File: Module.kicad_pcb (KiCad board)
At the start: 6 copper layers, 30 x 41.8 mm, 128 parts

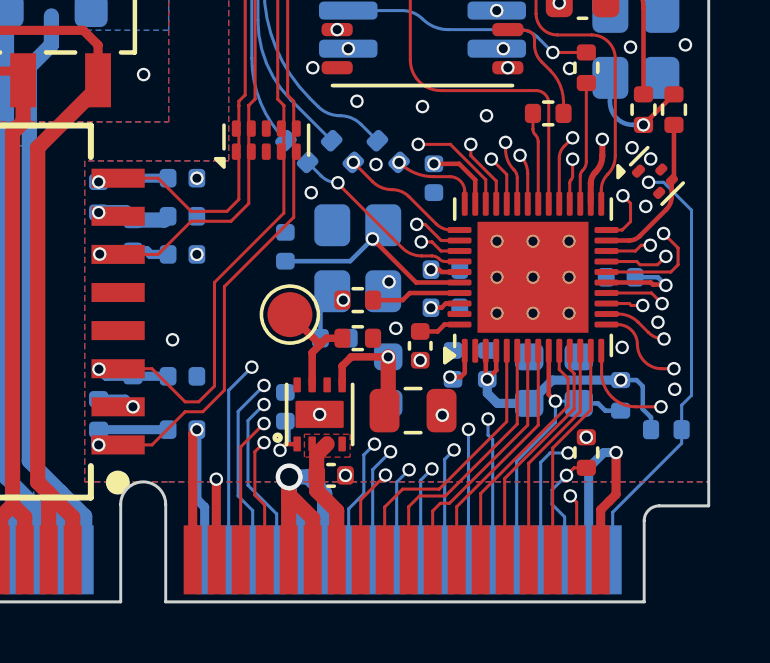
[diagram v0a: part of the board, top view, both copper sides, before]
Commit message: increased trace width from all goldfinger connector traces to 6mil reduced mask and paste reduction of 1U3 to 1mil
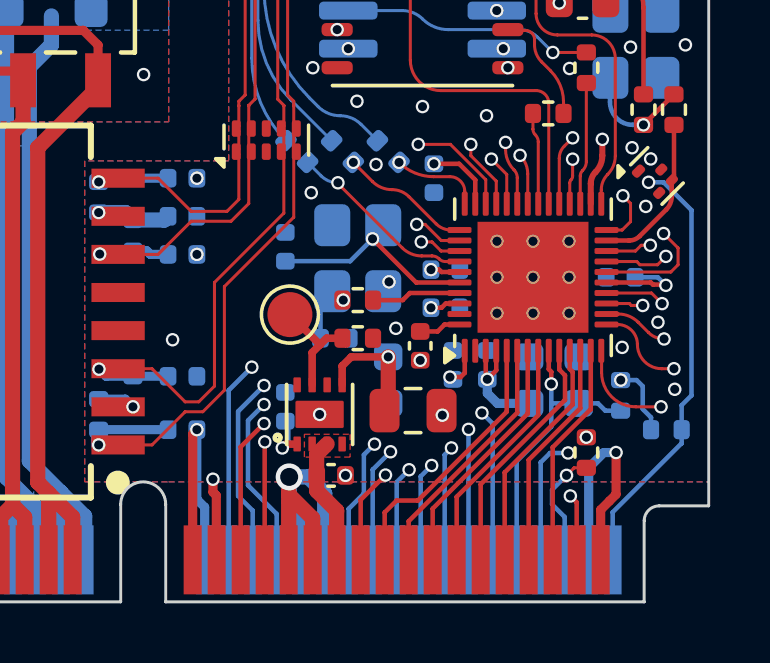
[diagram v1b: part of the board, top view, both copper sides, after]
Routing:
- net +3.3V: track 30.6 -> 27.2 mm
- net /GPIO37: track 8.98 -> 8.47 mm

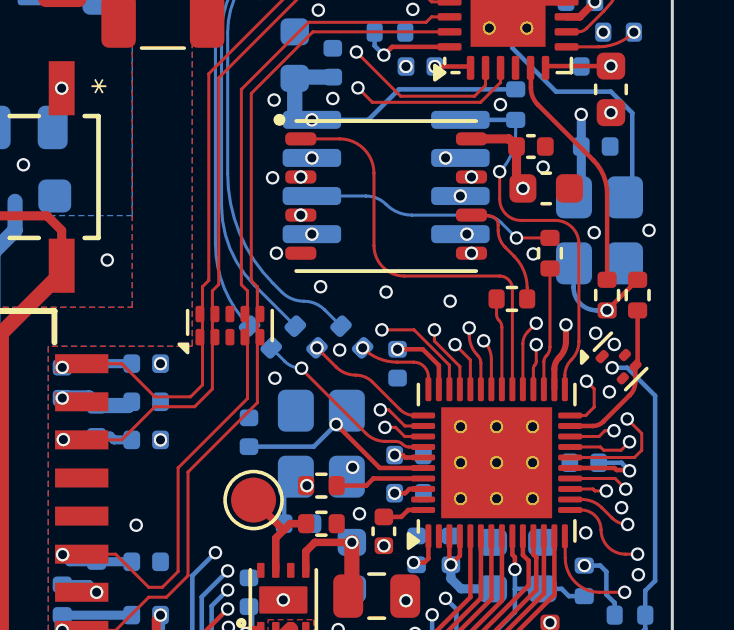
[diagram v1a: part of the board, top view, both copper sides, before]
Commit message: added testpoints to flash/ram signals
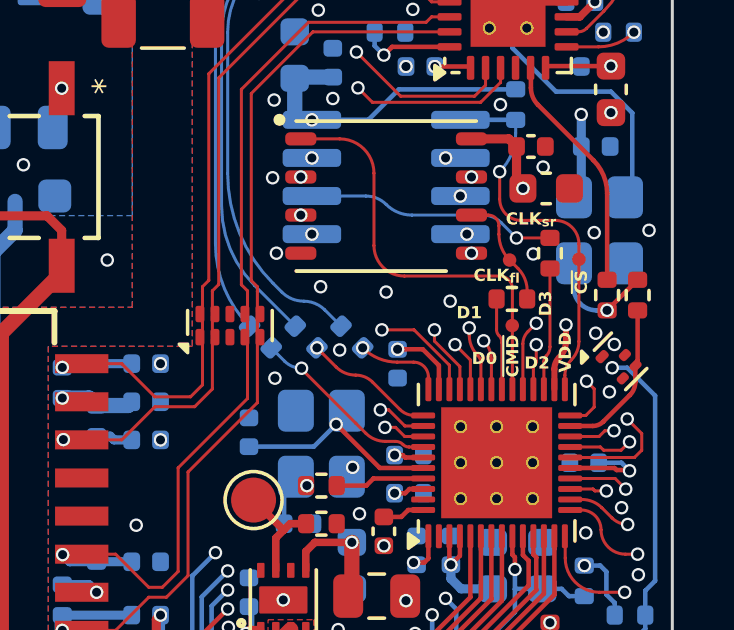
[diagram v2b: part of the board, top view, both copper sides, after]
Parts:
- added 1TP2: TestPoint, TestPoint:TestPoint_Pad_D1.0mm, F.Cu at (9.66, -12.2)
- added 1TP3: TestPoint, TestPoint:TestPoint_Pad_D1.0mm, F.Cu at (9.58, -14.4)
- added 1TP4: TestPoint, TestPoint:TestPoint_Pad_D1.0mm, F.Cu at (11.9, -14.4)
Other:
- board text added: "CLK_{fl}"
- board text added: "CLK_{sr}"
- board text added: "D0"
- board text added: "D1"
- board text added: "D2"
- board text added: "D3"
- board text added: "VDD"
- board text added: "~{CMD}"
- board text added: "~{CS}"

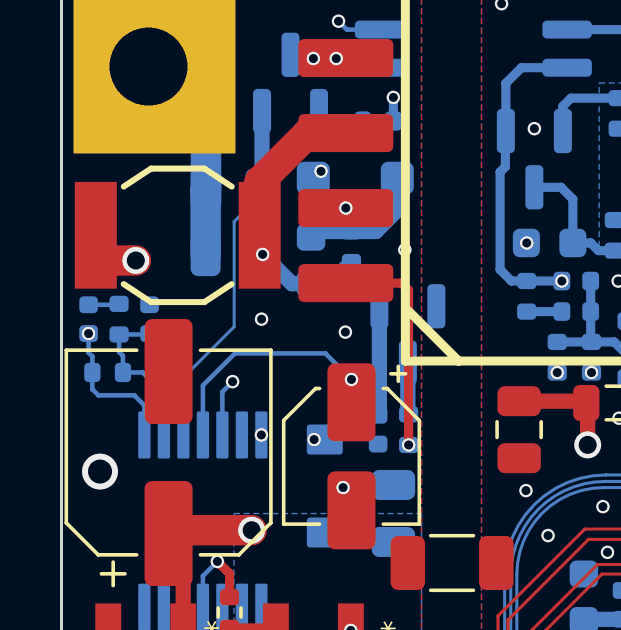
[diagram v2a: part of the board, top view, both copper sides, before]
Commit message: moved three 0402 resistors away from board edge
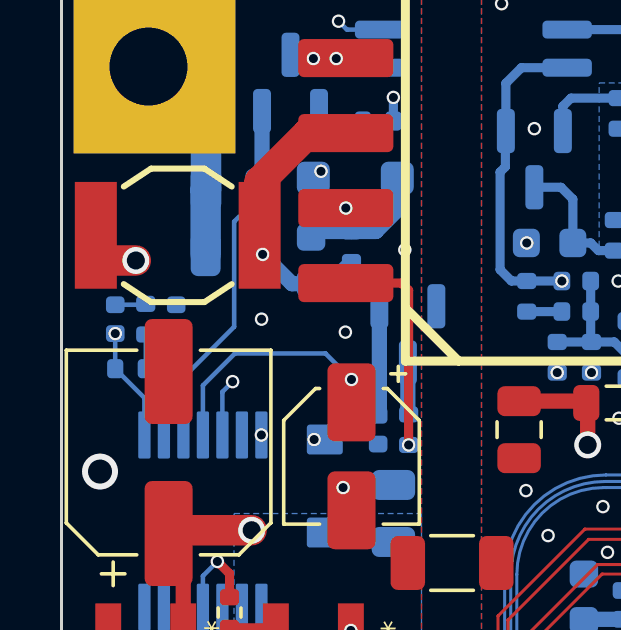
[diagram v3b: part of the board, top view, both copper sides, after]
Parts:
- moved 2C7 0.89 mm to (-11.2, -30.5)
- moved 2C8 0.89 mm to (-13.2, -30.5)
- moved 2R9 0.89 mm to (-12.2, -30.5)
- moved 2R12 0.77 mm to (-12.7, -28.8)
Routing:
- net Net-(2U2-CTL): track 23.3 -> 21.3 mm
- net Net-(2U2-VB): track 5.38 -> 4.63 mm
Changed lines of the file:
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@@
 	(footprint "Capacitor_SMD:C_0402_1005Metric"
 		(layer "B.Cu")
-		(at -14.097 -30.48 -90)
+		(at -13.208 -30.48 -90)
 		(descr "Capacitor SMD 0402 (1005 Metric), square (rectangular) end terminal, IPC-7351 nominal, (Body size source: IPC-SM-782 page 76, https://www.pcb-3d.com/wordpress/wp-content/uploads/ipc-sm-782a_amendment_1_and_2.pdf), generated with kicad-footprint-generator")
 		(tags "capacitor")
@@
 	(footprint "Resistor_SMD:R_0402_1005Metric"
 		(layer "B.Cu")
-		(at -13.081 -30.48 90)
+		(at -12.192 -30.48 90)
 		(descr "Resistor SMD 0402 (1005 Metric), square (rectangular) end terminal, IPC-7351 nominal, (Body size source: IPC-SM-782 page 72, https://www.pcb-3d.com/wordpress/wp-content/uploads/ipc-sm-782a_amendment_1_and_2.pdf), generated with kicad-footprint-generator")
 		(tags "resistor")
@@
 	(footprint "Capacitor_SMD:C_0402_1005Metric"
 		(layer "B.Cu")
-		(at -12.065 -30.48 90)
+		(at -11.176 -30.48 90)
 		(descr "Capacitor SMD 0402 (1005 Metric), square (rectangular) end terminal, IPC-7351 nominal, (Body size source: IPC-SM-782 page 76, https://www.pcb-3d.com/wordpress/wp-content/uploads/ipc-sm-782a_amendment_1_and_2.pdf), generated with kicad-footprint-generator")
 		(tags "capacitor")
 		(property "Reference" "2C7"
-			(at 2.12 0.165 90)
+			(at 0.0508 1.1176 90)
 			(layer "User.6")
 			(effects
@@
 	(footprint "Resistor_SMD:R_0402_1005Metric"
 		(layer "B.Cu")
-		(at -13.462 -28.702 180)
+		(at -12.7 -28.829 180)
 		(descr "Resistor SMD 0402 (1005 Metric), square (rectangular) end terminal, IPC-7351 nominal, (Body size source: IPC-SM-782 page 72, https://www.pcb-3d.com/wordpress/wp-content/uploads/ipc-sm-782a_amendment_1_and_2.pdf), generated with kicad-footprint-generator")
 		(tags "resistor")
@@
 		(tags "capacitor")
 		(property "Reference" "2C12"
-			(at 0.789 -0.921 0)
+			(at 2.286 -0.0254 0)
 			(layer "User.6")
 			(effects
@@
 	)
 	(segment
-		(start -12.2936 -28.702)
-		(end -12.952 -28.702)
+		(start -11.587 -28.226)
+		(end -12.19 -28.829)
 		(width 0.1524)
 		(layer "B.Cu")
@@
 	)
 	(segment
-		(start -11.587 -27.9954)
-		(end -12.2936 -28.702)
+		(start -12.19 -28.829)
+		(end -12.19 -29.968)
 		(width 0.1524)
 		(layer "B.Cu")
@@
 	)
 	(segment
-		(start -12.952 -29.2588)
-		(end -13.081 -29.3878)
+		(start -12.192 -29.97)
+		(end -11.206 -29.97)
 		(width 0.1524)
 		(layer "B.Cu")
@@
 	)
 	(segment
-		(start -13.081 -29.97)
-		(end -12.095 -29.97)
-		(width 0.1524)
-		(layer "B.Cu")
-		(net 85)
-	)
-	(segment
-		(start -12.095 -29.97)
-		(end -12.065 -30)
-		(width 0.1524)
-		(layer "B.Cu")
-		(net 85)
-	)
-	(segment
-		(start -12.952 -28.702)
-		(end -12.952 -29.2588)
+		(start -12.19 -29.968)
+		(end -12.192 -29.97)
 		(width 0.1524)
 		(layer "B.Cu")
@@
 	(segment
 		(start -11.587 -26.619)
-		(end -11.587 -27.9954)
+		(end -11.587 -28.226)
 		(width 0.1524)
 		(layer "B.Cu")
@@
 	)
 	(segment
-		(start -13.081 -29.3878)
-		(end -13.081 -29.97)
+		(start -11.206 -29.97)
+		(end -11.176 -30)
 		(width 0.1524)
 		(layer "B.Cu")
@@
 	)
 	(segment
-		(start -14.097 -30.96)
-		(end -13.111 -30.96)
+		(start -13.208 -30.96)
+		(end -12.222 -30.96)
 		(width 0.1524)
 		(layer "B.Cu")
@@
 	)
 	(segment
-		(start -13.111 -30.96)
-		(end -13.081 -30.99)
+		(start -12.222 -30.96)
+		(end -12.192 -30.99)
 		(width 0.1524)
 		(layer "B.Cu")
@@
 	)
 	(via
-		(at -5.7658 -40.4114)
+		(at -13.208 -30)
 		(size 0.45)
 		(drill 0.3)
@@
 	)
 	(via
-		(at -14.097 -30)
+		(at -5.7658 -40.4114)
 		(size 0.45)
 		(drill 0.3)
@@
 	)
 	(segment
-		(start -14.097 -29.3624)
-		(end -13.972 -29.2374)
-		(width 0.1524)
-		(layer "B.Cu")
-		(net 92)
-	)
-	(segment
-		(start -13.7668 -27.94)
-		(end -13.972 -28.1452)
-		(width 0.1524)
-		(layer "B.Cu")
-		(net 92)
-	)
-	(segment
-		(start -12.237 -27.604)
-		(end -12.573 -27.94)
+		(start -13.21 -28.829)
+		(end -13.21 -29.998)
 		(width 0.1524)
 		(layer "B.Cu")
@@
 	(segment
 		(start -12.237 -26.619)
-		(end -12.237 -27.604)
+		(end -12.237 -27.856)
 		(width 0.1524)
 		(layer "B.Cu")
@@
 	)
 	(segment
-		(start -14.097 -30)
-		(end -14.097 -29.3624)
+		(start -13.21 -29.998)
+		(end -13.208 -30)
 		(width 0.1524)
 		(layer "B.Cu")
@@
 	)
 	(segment
-		(start -13.972 -28.1452)
-		(end -13.972 -28.702)
-		(width 0.1524)
-		(layer "B.Cu")
-		(net 92)
-	)
-	(segment
-		(start -12.573 -27.94)
-		(end -13.7668 -27.94)
-		(width 0.1524)
-		(layer "B.Cu")
-		(net 92)
-	)
-	(segment
-		(start -13.972 -29.2374)
-		(end -13.972 -28.702)
+		(start -12.237 -27.856)
+		(end -13.21 -28.829)
 		(width 0.1524)
 		(layer "B.Cu")
@@
 	)
 	(segment
-		(start -7.366 -39.8272)
-		(end -7.366 -32.512)
+		(start -9.878 -30)
+		(end -13.208 -30)
 		(width 0.1524)
 		(layer "In3.Cu")
@@
 	)
 	(segment
-		(start -9.878 -30)
-		(end -14.097 -30)
+		(start -7.366 -39.8272)
+		(end -7.366 -32.512)
 		(width 0.1524)
 		(layer "In3.Cu")
@@
 		(start -9.2456 -33.7312)
 		(end -9.2456 -30.226)
-		(width 0.1016)
+		(width 0.1524)
 		(layer "B.Cu")
 		(net 109)
@@
 		(start -10.937 -28.5346)
 		(end -10.937 -26.619)
-		(width 0.1016)
+		(width 0.1524)
 		(layer "B.Cu")
 		(net 109)
@@
 		(start -8.3585 -34.6183)
 		(end -9.2456 -33.7312)
-		(width 0.1016)
+		(width 0.1524)
 		(layer "B.Cu")
 		(net 109)
@@
 		(start -9.2456 -30.226)
 		(end -10.937 -28.5346)
-		(width 0.1016)
+		(width 0.1524)
 		(layer "B.Cu")
 		(net 109)
@@
 		(min_thickness 0.0254)
 		(filled_areas_thickness no)
-		(fill
+		(fill yes
 			(thermal_gap 0.5)
 			(thermal_bridge_width 0.5)
@@
 		(min_thickness 0.25)
 		(filled_areas_thickness no)
-		(fill
+		(fill yes
 			(thermal_gap 0.5)
 			(thermal_bridge_width 0.5)
@@
 		(min_thickness 0.25)
 		(filled_areas_thickness no)
-		(fill
+		(fill yes
 			(thermal_gap 0.5)
 			(thermal_bridge_width 0.5)
@@
 		(min_thickness 0.25)
 		(filled_areas_thickness no)
-		(fill
+		(fill yes
 			(thermal_gap 0.5)
 			(thermal_bridge_width 0.5)
@@
 		(min_thickness 0.25)
 		(filled_areas_thickness no)
-		(fill
+		(fill yes
 			(thermal_gap 0.5)
 			(thermal_bridge_width 0.5)
@@
 		(min_thickness 0.2)
 		(filled_areas_thickness no)
-		(fill
+		(fill yes
 			(thermal_gap 0.5)
 			(thermal_bridge_width 0.5)
@@
 		(min_thickness 0.1)
 		(filled_areas_thickness no)
-		(fill
+		(fill yes
 			(thermal_gap 0.5)
 			(thermal_bridge_width 0.5)
@@
 		(min_thickness 0.25)
 		(filled_areas_thickness no)
-		(fill
+		(fill yes
 			(thermal_gap 0.5)
 			(thermal_bridge_width 0.5)
@@
 		(min_thickness 0.25)
 		(filled_areas_thickness no)
-		(fill
+		(fill yes
 			(thermal_gap 0.5)
 			(thermal_bridge_width 0.5)

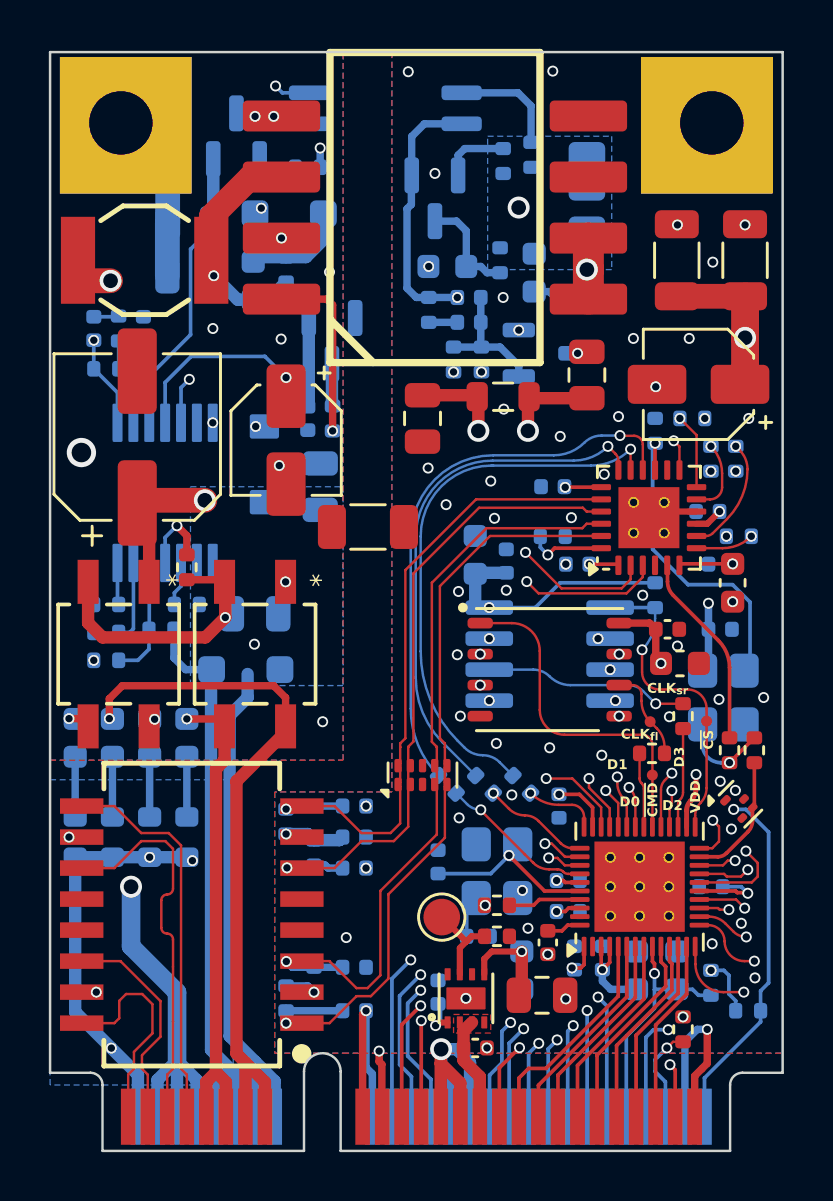
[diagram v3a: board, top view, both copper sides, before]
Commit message: added test points for PoE stage
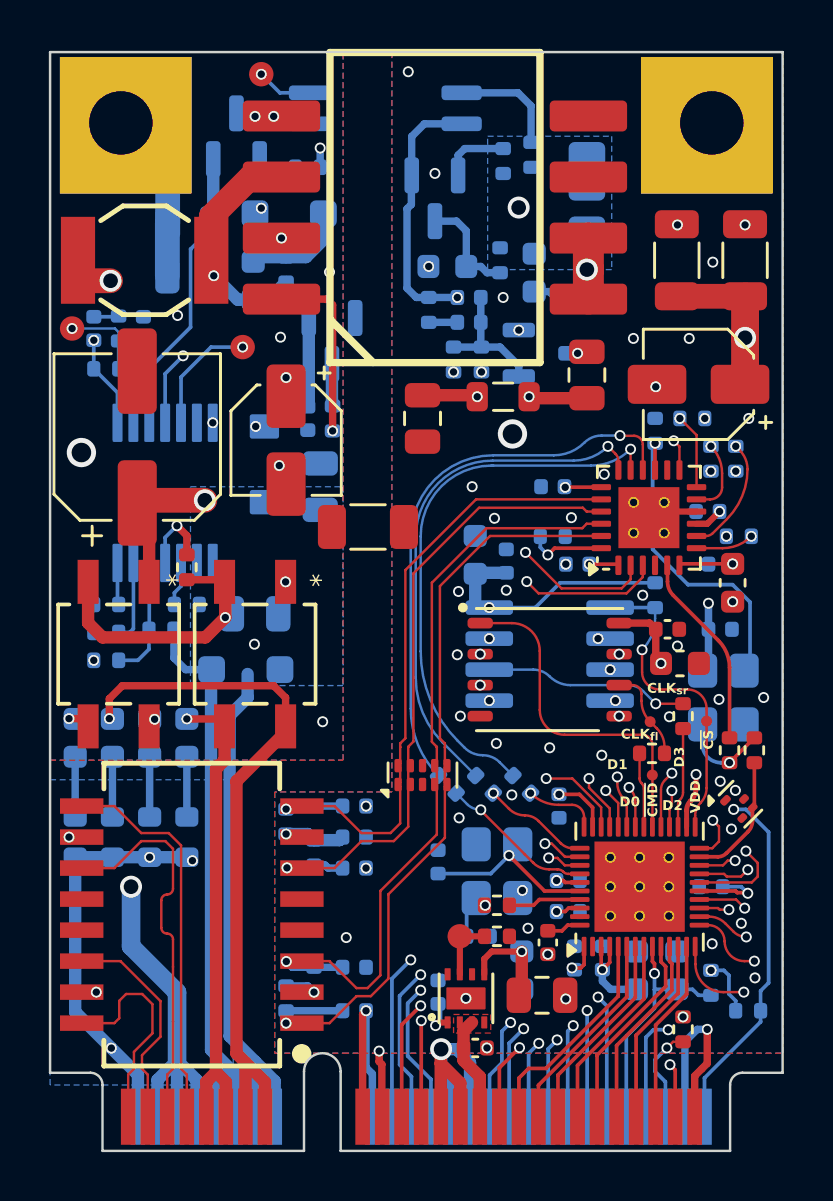
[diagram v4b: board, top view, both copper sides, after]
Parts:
- added 1TP5: TestPoint, TestPoint:TestPoint_Pad_D1.0mm, F.Cu at (-14.1, -30.5)
- added 1TP7: TestPoint, TestPoint:TestPoint_Pad_D1.0mm, F.Cu at (-7.11, -29.7)
- added 1TP8: TestPoint, TestPoint:TestPoint_Pad_D1.0mm, F.Cu at (-6.35, -40.9)
- 1TP1: footprint TestPoint:TestPoint_Pad_D1.5mm -> TestPoint:TestPoint_Pad_D1.0mm
- moved 1TP1 1.08 mm to (1.78, -5.59)
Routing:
- net Net-(2U2-VB): track 4.63 -> 6.96 mm, vias 0 -> 1
- net +3.3V: track 27.2 -> 25.8 mm
- net +3.3VA: track 53.3 -> 54.5 mm
- net Net-(1U5-ILM): track 3.70 -> 2.57 mm
- net Net-(2U2-GATE): track 14.4 -> 15.2 mm
- net Net-(2D4-K): track 12.0 -> 12.2 mm, vias 1 -> 2
- net GND: vias 56 -> 51

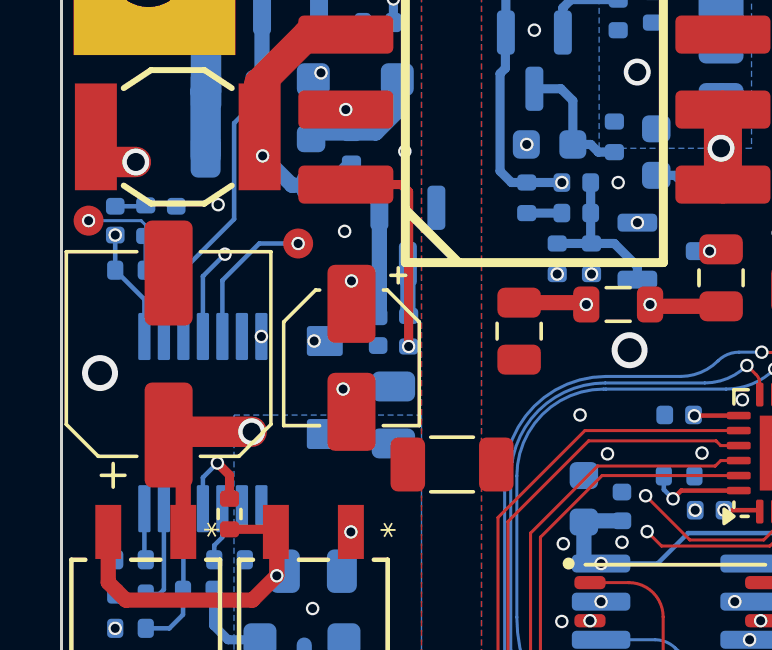
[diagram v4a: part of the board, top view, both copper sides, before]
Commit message: fixed 2D4 polarity orientation and footprint
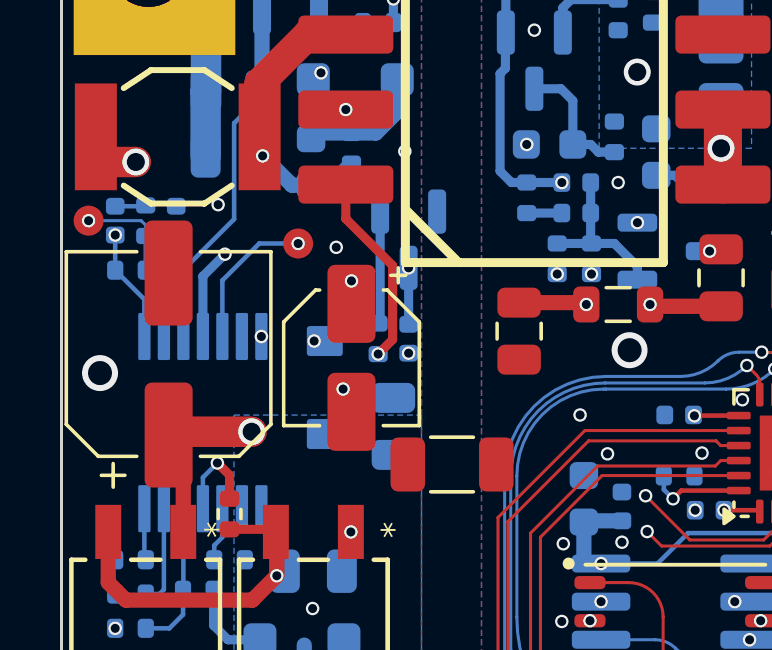
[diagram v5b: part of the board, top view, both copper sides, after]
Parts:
- 2D4: footprint Project:SOT-23-BAS16 -> Package_TO_SOT_SMD:SOT-23
- moved 2C9 1.05 mm to (-3.43, -26.5)
- moved 2R14 1.05 mm to (-4.45, -26.5)
- moved 2C11 0.38 mm to (-3.94, -23.6)
- moved 2D4 0.13 mm to (-3.43, -29.8)
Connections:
- 2D4 pad 1: Net-(2D4-K) -> Net-(2D4-A)
- 2D4 pad 2: Net-(2D4-A) -> unconnected-(2D4-NC-Pad2)
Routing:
- net Net-(2D4-A): track 1.74 -> 3.76 mm
- net Net-(1T1-Pad1): track 7.35 -> 6.50 mm
- net Net-(2D4-K): track 12.2 -> 11.6 mm, vias 2 -> 3
- net GNDPWR: vias 10 -> 11
